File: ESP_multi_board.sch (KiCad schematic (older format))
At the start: 14 parts

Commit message: Reg5Vto3.3V añadido como hoja jerarquica, añadido conector I2C externo, añadido resistencia ESP
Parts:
- removed U?: LM2931Z-3.3/5.0, TO92-123, symbol LM2931Z-3.3/5.0
- added IC?: L293D, stepper drivers-DIL16, symbol L293D
- added JUMPER? (x2), P? (x2): CONN_01X02, symbol CONN_01X02
- added P? (x2): CONN_01X06, symbol CONN_01X06
- added P?: CONN_01X12, symbol CONN_01X12
- added P?: CONN_01X08, symbol CONN_01X08
- added P?: CONN_I2C, symbol CONN_01X04
- added R?: 10k, symbol R
- added R?: R, symbol R
- added R? (x2): 47k, symbol R
- added U?: ESP-12, symbol ESP-12
- added U?: MPU-6050, symbol MPU-6050
- added U?: MCP23008, symbol MCP23008
- added U?: MAX11605EEE+, symbol MAX11605EEE+
- P?: value CONN_01X06 -> CONN_M2
- P?: value CONN_01X06 -> CONN_M1
- P?: value CONN_01X12 -> CONN_Ain
- P?: value CONN_01X08 -> CONN_DIGITAL
- P?: value CONN_01X02 -> CONN_BATERIA2
- P?: value CONN_01X02 -> CONN_BATERIA1
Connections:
- net labels added: AinRaw, RX, TX
- wire segments 52 -> 61
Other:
- moved on the sheet: P?

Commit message: incluido conectores I2C externos para el MPU6050\n modificado JUMPER1
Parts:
- removed JUMPER1, JUMPER2, JUMPER? (x2): CONN_01X02, symbol CONN_01X02
- removed U? (x2): MPU-6050, symbol MPU-6050
- added P?: CONN_I2C_MPU6050, symbol CONN_01X08
- added P?: JUMPER1, symbol CONN_01X03
- R?: value R -> 10k
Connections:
- net labels added: INT_MPU6050, XCL, XDA
- wire segments 61 -> 63
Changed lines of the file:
@@
-$EndComp
-$Comp
-L MPU-6050 U?
-U 1 1 570EA5C6
-P 9200 4750
-F 0 "U?" H 9550 4050 60  0000 C CNN
-F 1 "MPU-6050" H 8950 4050 60  0000 C CNN
-F 2 "" H 9200 4500 60  0000 C CNN
-F 3 "" H 9200 4500 60  0000 C CNN
-	1    9200 4750
-	1    0    0    -1
 $EndComp
 $Comp
@@
 $Comp
 L GND #PWR?
-U 1 1 570EB715
-P 8400 4500
-F 0 "#PWR?" H 8400 4250 50  0001 C CNN
-F 1 "GND" H 8400 4350 50  0000 C CNN
-F 2 "" H 8400 4500 50  0000 C CNN
-F 3 "" H 8400 4500 50  0000 C CNN
-	1    8400 4500
-	0    1    1    0
-$EndComp
-$Comp
-L GND #PWR?
 U 1 1 570EB827
 P 1200 4550
@@
 Text GLabel 9150 1350 2    60   BiDi ~ 0
 VDD
-Text GLabel 8400 3950 0    60   BiDi ~ 0
-VDD
-Text GLabel 9950 3950 2    60   BiDi ~ 0
-SCL
-Text GLabel 9950 4050 2    60   BiDi ~ 0
-SDA
 Text GLabel 7750 1450 0    60   BiDi ~ 0
 SDA
@@
 Text GLabel 7750 1550 0    60   BiDi ~ 0
 VDD
-$Comp
-L CONN_01X02 JUMPER1
-U 1 1 570ECE84
-P 7350 2250
-F 0 "JUMPER1" H 7350 2400 50  0000 C CNN
-F 1 "CONN_01X02" V 7450 2250 50  0000 C CNN
-F 2 "" H 7350 2250 50  0000 C CNN
-F 3 "" H 7350 2250 50  0000 C CNN
-	1    7350 2250
-	0    1    1    0
-$EndComp
-Text GLabel 7300 2050 1    60   BiDi ~ 0
-GPIO0
 Text GLabel 6200 2350 2    60   BiDi ~ 0
 GPIO0
@@
 	-1   0    0    1
 $EndComp
-$Comp
-L CONN_01X02 JUMPER2
-U 1 1 570ED5A9
-P 7350 2550
-F 0 "JUMPER2" H 7350 2700 50  0000 C CNN
-F 1 "CONN_01X02" V 7450 2550 50  0000 C CNN
-F 2 "" H 7350 2550 50  0000 C CNN
-F 3 "" H 7350 2550 50  0000 C CNN
-	1    7350 2550
-	0    -1   -1   0
-$EndComp
-Text GLabel 7400 2750 3    60   BiDi ~ 0
-ENC2_A
-Text GLabel 7300 2750 3    60   BiDi ~ 0
-GPIO0
 Text GLabel 6200 2450 2    60   BiDi ~ 0
 ENC1_A
@@
 	9850 1450 9150 1450
 Wire Wire Line
-	7750 2050 7400 2050
+	7750 2050 7300 2050
 Wire Wire Line
 	1200 2350 1500 2350
@@
 $EndComp
 $Comp
-L MPU-6050 U?
-U 1 1 57125BD3
-P 9200 4750
-F 0 "U?" H 9550 4050 60  0000 C CNN
-F 1 "MPU-6050" H 8950 4050 60  0000 C CNN
-F 2 "" H 9200 4500 60  0000 C CNN
-F 3 "" H 9200 4500 60  0000 C CNN
-	1    9200 4750
-	1    0    0    -1
-$EndComp
-$Comp
 L MCP23008 U?
 U 1 1 57125BD4
@@
 $Comp
 L GND #PWR?
-U 1 1 57125BD8
-P 8400 4500
-F 0 "#PWR?" H 8400 4250 50  0001 C CNN
-F 1 "GND" H 8400 4350 50  0000 C CNN
-F 2 "" H 8400 4500 50  0000 C CNN
-F 3 "" H 8400 4500 50  0000 C CNN
-	1    8400 4500
-	0    1    1    0
-$EndComp
-$Comp
-L GND #PWR?
 U 1 1 57125BD9
 P 1200 4550
@@
 Text GLabel 9150 1350 2    60   BiDi ~ 0
 VDD
-Text GLabel 8400 3950 0    60   BiDi ~ 0
-VDD
-Text GLabel 9950 3950 2    60   BiDi ~ 0
-SCL
-Text GLabel 9950 4050 2    60   BiDi ~ 0
-SDA
 Text GLabel 7750 1450 0    60   BiDi ~ 0
 SDA
@@
 Text GLabel 7750 1550 0    60   BiDi ~ 0
 VDD
-$Comp
-L CONN_01X02 JUMPER?
-U 1 1 57125BE3
-P 7350 2250
-F 0 "JUMPER?" H 7350 2400 50  0000 C CNN
-F 1 "CONN_01X02" V 7450 2250 50  0000 C CNN
-F 2 "" H 7350 2250 50  0000 C CNN
-F 3 "" H 7350 2250 50  0000 C CNN
-	1    7350 2250
-	0    1    1    0
-$EndComp
-Text GLabel 7300 2050 1    60   BiDi ~ 0
-GPIO0
 Text GLabel 6200 2350 2    60   BiDi ~ 0
 GPIO0
@@
 	-1   0    0    1
 $EndComp
-$Comp
-L CONN_01X02 JUMPER?
-U 1 1 57125BEA
-P 7350 2550
-F 0 "JUMPER?" H 7350 2700 50  0000 C CNN
-F 1 "CONN_01X02" V 7450 2550 50  0000 C CNN
-F 2 "" H 7350 2550 50  0000 C CNN
-F 3 "" H 7350 2550 50  0000 C CNN
-	1    7350 2550
-	0    -1   -1   0
-$EndComp
-Text GLabel 7400 2750 3    60   BiDi ~ 0
-ENC2_A
-Text GLabel 7300 2750 3    60   BiDi ~ 0
-GPIO0
 Text GLabel 6200 2450 2    60   BiDi ~ 0
 ENC1_A
@@
 P 4100 1850
 F 0 "R?" V 4180 1850 50  0000 C CNN
-F 1 "R" V 4100 1850 50  0000 C CNN
+F 1 "10k" V 4100 1850 50  0000 C CNN
 F 2 "" V 4030 1850 50  0000 C CNN
 F 3 "" H 4100 1850 50  0000 C CNN
@@
 $EndComp
 Wire Wire Line
-	10100 3000 10600 3000
+	10100 3000 10500 3000
+Wire Wire Line
+	10500 3000 10600 3000
 Wire Wire Line
 	10500 3000 10500 3100
@@
 $EndComp
 Wire Wire Line
-	10100 2900 10600 2900
+	10100 2900 10300 2900
+Wire Wire Line
+	10300 2900 10600 2900
 Wire Wire Line
 	10300 2900 10300 3050
@@
 Text GLabel 10600 2700 0    60   BiDi ~ 0
 VDD
+$Comp
+L CONN_01X08 P?
+U 1 1 5713D03F
+P 8450 4950
+F 0 "P?" H 8450 5400 50  0000 C CNN
+F 1 "CONN_I2C_MPU6050" V 8550 4950 50  0000 C CNN
+F 2 "" H 8450 4950 50  0000 C CNN
+F 3 "" H 8450 4950 50  0000 C CNN
+	1    8450 4950
+	0    1    1    0
+$EndComp
+Text GLabel 8100 4750 1    60   BiDi ~ 0
+VDD
+Text GLabel 8300 4750 1    60   BiDi ~ 0
+SCL
+Text GLabel 8400 4750 1    60   BiDi ~ 0
+SDA
+Text GLabel 8500 4750 1    60   BiDi ~ 0
+XDA
+Text GLabel 8600 4750 1    60   BiDi ~ 0
+XCL
+Text GLabel 8800 4750 1    60   BiDi ~ 0
+INT_MPU6050
+$Comp
+L GND #PWR?
+U 1 1 5713D47A
+P 8200 4750
+F 0 "#PWR?" H 8200 4500 50  0001 C CNN
+F 1 "GND" H 8200 4600 50  0000 C CNN
+F 2 "" H 8200 4750 50  0000 C CNN
+F 3 "" H 8200 4750 50  0000 C CNN
+	1    8200 4750
+	-1   0    0    1
+$EndComp
+$Comp
+L GND #PWR?
+U 1 1 5713D831
+P 8700 4750
+F 0 "#PWR?" H 8700 4500 50  0001 C CNN
+F 1 "GND" H 8700 4600 50  0000 C CNN
+F 2 "" H 8700 4750 50  0000 C CNN
+F 3 "" H 8700 4750 50  0000 C CNN
+	1    8700 4750
+	-1   0    0    1
+$EndComp
+$Comp
+L CONN_01X03 P?
+U 1 1 5713DB4D
+P 7200 1850
+F 0 "P?" H 7200 2050 50  0000 C CNN
+F 1 "JUMPER1" V 7300 1850 50  0000 C CNN
+F 2 "" H 7200 1850 50  0000 C CNN
+F 3 "" H 7200 1850 50  0000 C CNN
+	1    7200 1850
+	0    -1   -1   0
+$EndComp
+Text GLabel 7200 2050 3    60   BiDi ~ 0
+GPIO0
+Text GLabel 7100 2050 3    60   BiDi ~ 0
+ENC2_A
+Text GLabel 7750 1850 0    60   BiDi ~ 0
+VDD
 $EndSCHEMATC

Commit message: modificado jumper1
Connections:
- net ENC2_A: now also U?.10 (GPIO15), U?.10 (GPIO15); no longer P?.1 (P1)
- net INT_MPU6050: no longer names the net of P?.1 (P1)
- net INT_MPU6050: now also P?.1 (P1)
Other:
- moved on the sheet: P?
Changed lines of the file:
@@
 	-1   0    0    1
 $EndComp
-Text GLabel 6200 2450 2    60   BiDi ~ 0
-ENC1_A
 Text GLabel 4400 2250 0    60   BiDi ~ 0
 M1_A
@@
 	9850 1450 9150 1450
 Wire Wire Line
-	7750 2050 7300 2050
+	7600 2050 7600 3100
 Wire Wire Line
 	1200 2350 1500 2350
@@
 	-1   0    0    1
 $EndComp
-Text GLabel 6200 2450 2    60   BiDi ~ 0
-ENC1_A
 Text GLabel 4400 2250 0    60   BiDi ~ 0
 M1_A
@@
 $EndComp
 Wire Wire Line
-	10100 3000 10500 3000
-Wire Wire Line
-	10500 3000 10600 3000
+	10100 3000 10600 3000
 Wire Wire Line
 	10500 3000 10500 3100
@@
 $EndComp
 Wire Wire Line
-	10100 2900 10300 2900
-Wire Wire Line
-	10300 2900 10600 2900
+	10100 2900 10600 2900
 Wire Wire Line
 	10300 2900 10300 3050
@@
 Text GLabel 8600 4750 1    60   BiDi ~ 0
 XCL
-Text GLabel 8800 4750 1    60   BiDi ~ 0
-INT_MPU6050
 $Comp
 L GND #PWR?
@@
 L CONN_01X03 P?
 U 1 1 5713DB4D
-P 7200 1850
-F 0 "P?" H 7200 2050 50  0000 C CNN
-F 1 "JUMPER1" V 7300 1850 50  0000 C CNN
-F 2 "" H 7200 1850 50  0000 C CNN
-F 3 "" H 7200 1850 50  0000 C CNN
-	1    7200 1850
-	0    -1   -1   0
-$EndComp
-Text GLabel 7200 2050 3    60   BiDi ~ 0
+P 7400 3200
+F 0 "P?" H 7400 3400 50  0000 C CNN
+F 1 "JUMPER1" V 7500 3200 50  0000 C CNN
+F 2 "" H 7400 3200 50  0000 C CNN
+F 3 "" H 7400 3200 50  0000 C CNN
+	1    7400 3200
+	-1   0    0    1
+$EndComp
+Text GLabel 7600 3200 2    60   BiDi ~ 0
 GPIO0
-Text GLabel 7100 2050 3    60   BiDi ~ 0
+Text GLabel 7750 1850 0    60   BiDi ~ 0
+VDD
+Text GLabel 6200 2550 2    60   Input ~ 0
 ENC2_A
-Text GLabel 7750 1850 0    60   BiDi ~ 0
-VDD
+Text GLabel 6200 2450 2    60   Input ~ 0
+ENC1_A
+Wire Wire Line
+	7600 2050 7750 2050
+Wire Wire Line
+	7600 3300 8800 3300
+Wire Wire Line
+	8800 3300 8800 4750
 $EndSCHEMATC

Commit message: resueltos probelams con duplicados y checkeado esquematico
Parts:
- removed IC?: L293D, stepper drivers-DIL16, symbol L293D
- removed P?: CONN_M2, symbol CONN_01X06
- removed P?: CONN_M1, symbol CONN_01X06
- removed P?: CONN_Ain, symbol CONN_01X12
- removed P?: CONN_BATERIA2, symbol CONN_01X02
- removed P?: CONN_BATERIA1, symbol CONN_01X02
- removed P?: CONN_01X08, symbol CONN_01X08
- removed U?: ESP-12, symbol ESP-12
- removed U?: MCP23008, symbol MCP23008
- removed U?: MAX11605EEE+, symbol MAX11605EEE+
- added P106, P109, P110: CONN_01X03, symbol CONN_01X03
- P111: renamed from P?; symbol CONN_01X08 -> CONN_01X10
- gave numbers to parts that had none: 16
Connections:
- net M1_EN is gone; now on net VDD: IC101.1 (1,2EN)
- net M2_EN is gone; now on net VDD: IC101.9 (3,4EN)
- net ENC1_B: now also P109.3 (P3)
- net ENC2_B: now also P110.3 (P3)
- net GND: now also P111.2 (P2), U103.9 (VSS), P106.2 (P2)
- net RX: now also P106.3 (P3)
- net TX: now also P106.1 (P1)
- net VDD: now also P111.1 (P1)
- net at P111.8 (P8): now also U103.12 (GP2); no longer U103.10 (GP0)
- net at P111.7 (P7): now also U103.13 (GP3); no longer U103.11 (GP1)
- net at P111.6 (P6): now also U103.14 (GP4); no longer U103.12 (GP2)
- net at P111.5 (P5): now also U103.15 (GP5); no longer U103.13 (GP3)
- net at P111.4 (P4): now also U103.16 (GP6); no longer U103.14 (GP4)
- net at P111.3 (P3): now also U103.17 (GP7); no longer U103.15 (GP5)
- new net: P109.1 (P1), P111.10 (P10)
- new net: P110.1 (P1), P111.9 (P9)
- new net: P109.2 (P2), U103.10 (GP0)
- new net: P110.2 (P2), U103.11 (GP1)
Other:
- moved on the sheet: P103

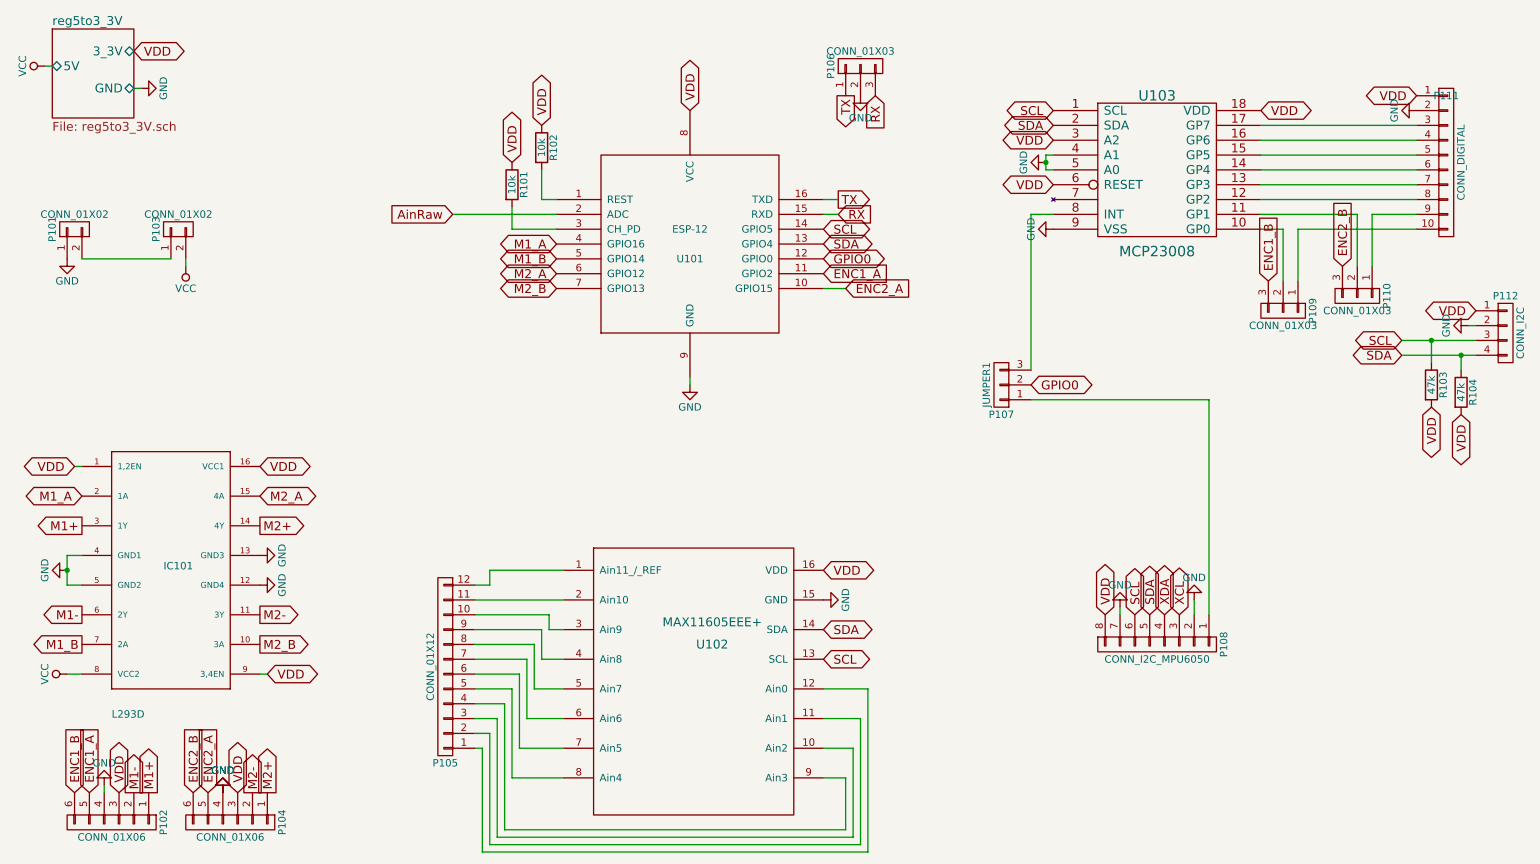
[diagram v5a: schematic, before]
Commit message: nuevo componente diseñado L293DD, asignadas huellas
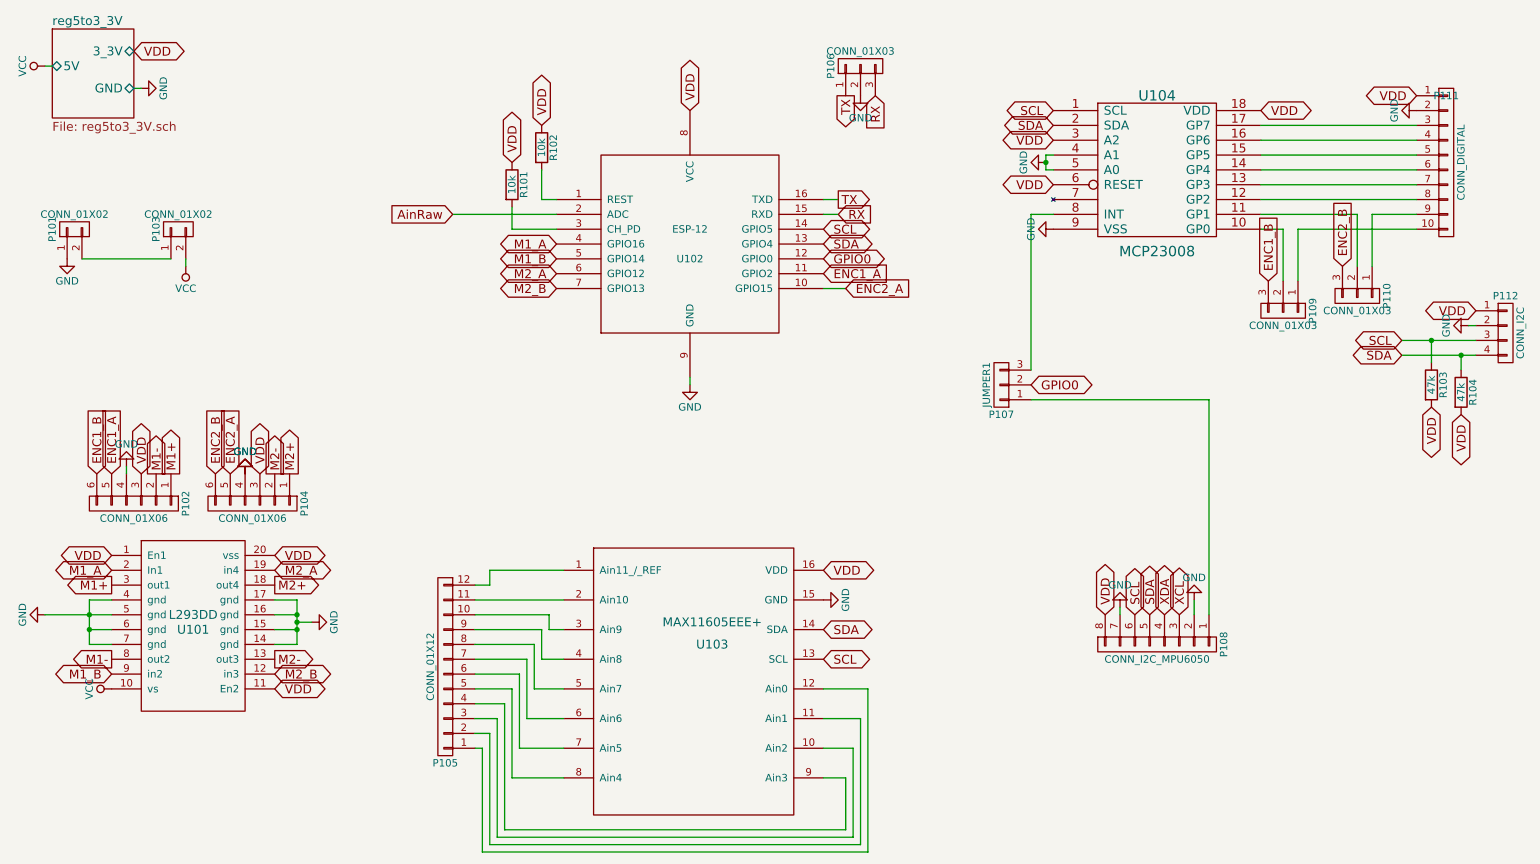
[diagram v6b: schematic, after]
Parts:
- removed IC101: L293D, stepper drivers-DIL16, symbol L293D
- added U101: L293DD, Housings_SOIC:SOIC-20_7.5x12.8mm_Pitch1.27mm, symbol L293DD
- P101, P103: footprint (none) -> Pin_Headers:Pin_Header_Angled_1x02
- P102, P104: footprint (none) -> Pin_Headers:Pin_Header_Straight_1x06
- P105: footprint (none) -> Pin_Headers:Pin_Header_Straight_1x12
- P106, P107, P109, P110: footprint (none) -> Pin_Headers:Pin_Header_Straight_1x03
- P108: footprint (none) -> Pin_Headers:Pin_Header_Straight_1x08
- P111: footprint (none) -> Pin_Headers:Pin_Header_Straight_1x10
- P112: footprint (none) -> Pin_Headers:Pin_Header_Straight_1x04
- R101, R102, R103, R104: footprint (none) -> Resistors_SMD:R_0402
- U102: renamed from U101; footprint (none) -> ESP8266:ESP-12
- U103: renamed from U102; footprint (none) -> Housings_SSOP:QSOP-16_3.9x4.9mm_Pitch0.635mm
- U104: renamed from U103; footprint (none) -> Housings_SOIC:SOIC-18_7.5x11.6mm_Pitch1.27mm
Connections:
- net GND: now also U101.14 (gnd), U101.15 (gnd), U101.16 (gnd), U101.17 (gnd), U101.4 (gnd), U101.5 (gnd), U101.6 (gnd), U101.7 (gnd)
- net M1+: now also U101.3 (out1)
- net M1-: now also U101.8 (out2)
- net M1_A: now also U101.2 (In1)
- net M1_B: now also U101.9 (in2)
- net M2+: now also U101.18 (out4)
- net M2-: now also U101.13 (out3)
- net M2_A: now also U101.19 (in4)
- net M2_B: now also U101.12 (in3)
- net VCC: now also U101.10 (vs)
- net VDD: now also U101.1 (En1), U101.11 (En2), U101.20 (vss)
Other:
- moved on the sheet: P102, P104

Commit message: pendiente de enrutar, TODO: incluir diodos baterias, meditar los jumpers
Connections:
- net at U103.10 (Ain2): now also P105.2 (P2); no longer P105.3 (P3)
- net at U103.11 (Ain1): now also P105.3 (P3); no longer P105.2 (P2)
- net at U103.12 (Ain0): now also P105.4 (P4); no longer P105.1 (P1)
- net at U103.9 (Ain3): now also P105.1 (P1); no longer P105.4 (P4)
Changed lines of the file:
@@
 	4050 6200 6350 6200
 Wire Wire Line
-	6350 6200 6350 5850
-Wire Wire Line
-	6350 5850 6200 5850
+	6350 6200 6350 5250
 Wire Wire Line
 	3850 5450 4000 5450
@@
 	4000 6250 6400 6250
 Wire Wire Line
-	6400 6250 6400 5650
-Wire Wire Line
-	6400 5650 6200 5650
+	6400 6250 6400 5450
 Wire Wire Line
 	3950 5550 3950 6300
@@
 	3950 6300 6450 6300
 Wire Wire Line
-	6450 6300 6450 5450
+	6450 6300 6450 5650
 Wire Wire Line
-	6450 5450 6200 5450
-Wire Wire Line
-	6200 5250 6500 5250
-Wire Wire Line
-	6500 5250 6500 6350
+	6500 5850 6500 6350
 Wire Wire Line
 	6500 6350 3900 6350
@@
 VDD
 Wire Wire Line
-	1400 4950 1250 4950
+	1250 4950 1400 4950
 Wire Wire Line
-	1250 4950 1250 4650
+	1250 4650 1250 4950
 Wire Wire Line
 	1250 4650 1400 4650
@@
 	1400 4850 1250 4850
 Connection ~ 1250 4850
+Wire Wire Line
+	6350 5250 6200 5250
+Wire Wire Line
+	6400 5450 6200 5450
+Wire Wire Line
+	6450 5650 6200 5650
+Wire Wire Line
+	6500 5850 6200 5850
 $EndSCHEMATC
